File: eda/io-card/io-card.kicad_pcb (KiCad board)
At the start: 2 copper layers, 230 x 100 mm, 67 parts, among them J1 PS2, J2 Conn_02x25_Odd_Even, J3 PortA, J4 PortB, J5 ControlLines, J6 SPI, J7 Keyboard connector, J8 SD-Card module, J9 SD_Card, U1 W65C22SxP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

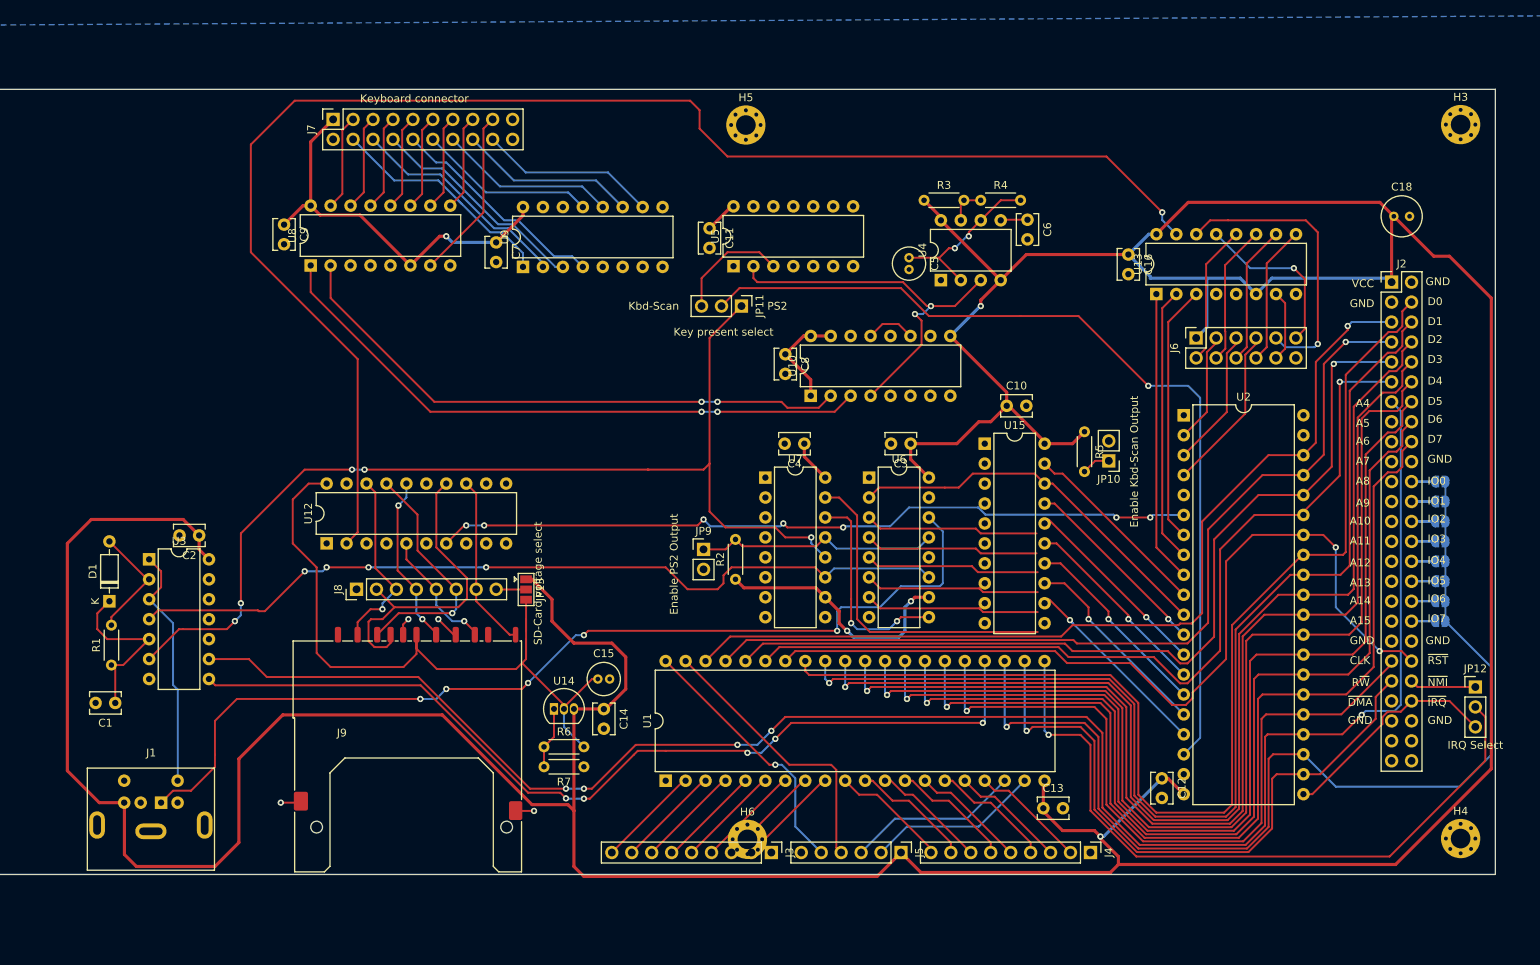
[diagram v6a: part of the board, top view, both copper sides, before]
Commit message: Rerouting IO card
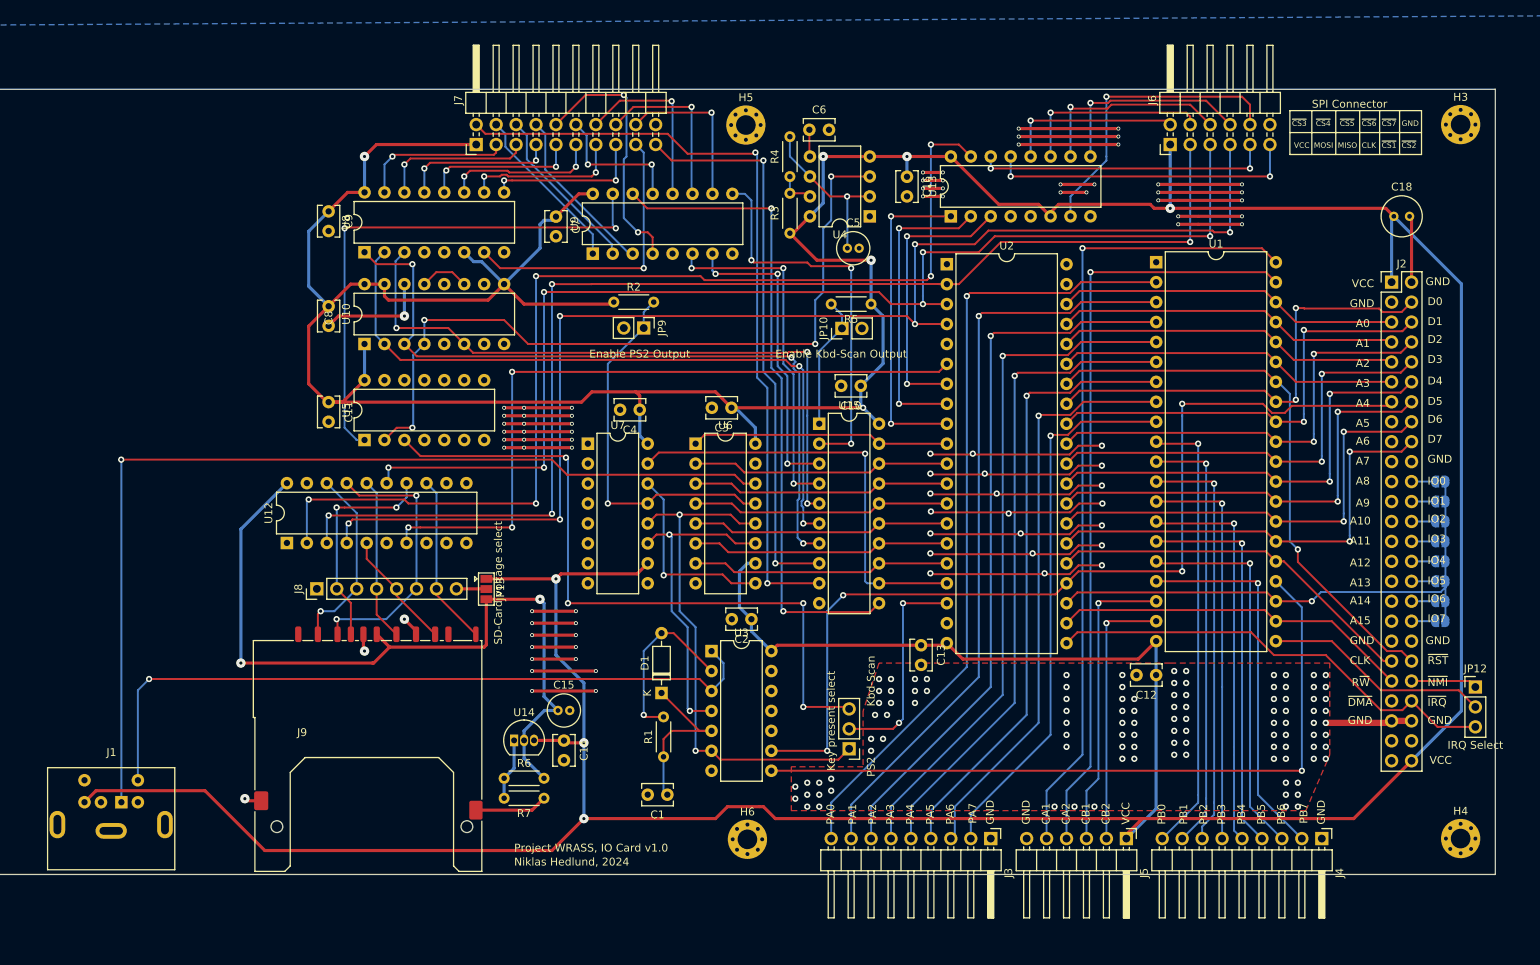
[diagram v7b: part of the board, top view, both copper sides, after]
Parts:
- J3, J4: footprint Connector_PinHeader_2.54mm:PinHeader_1x09_P2.54mm_Vertical -> Connector_PinHeader_2.54mm:PinHeader_1x09_P2.54mm_Horizontal
- J5: footprint Connector_PinHeader_2.54mm:PinHeader_1x06_P2.54mm_Vertical -> Connector_PinHeader_2.54mm:PinHeader_1x06_P2.54mm_Horizontal
- J6: footprint Connector_PinSocket_2.54mm:PinSocket_2x06_P2.54mm_Vertical -> Connector_PinHeader_2.54mm:PinHeader_2x06_P2.54mm_Horizontal
- J7: footprint Connector_PinSocket_2.54mm:PinSocket_2x10_P2.54mm_Vertical -> Connector_PinHeader_2.54mm:PinHeader_2x10_P2.54mm_Horizontal
- moved U1 90.9 mm to (202.9, 69.3), turned to 0 degrees
- moved U3 72.6 mm to (146.3, 118.9)
- moved D1 71.3 mm to (139.9, 124.2)
- moved C1 71.3 mm to (140.7, 137.2)
- moved R1 71.3 mm to (140.2, 132.3)
- moved C2 71.1 mm to (151.4, 114.8)
- moved C8 58.5 mm to (97.5, 75.0)
- moved JP11 58.0 mm to (163.8, 131.3), turned to 180 degrees
- moved U10 57.2 mm to (102.1, 79.8)
- moved C11 53.3 mm to (97.5, 87.2)
- moved U5 51.9 mm to (102.1, 92.0)
- moved R2 38.6 mm to (133.9, 74.4), turned to 0 degrees
- moved JP10 37.9 mm to (162.9, 77.8), turned to 90 degrees
- moved U2 35.8 mm to (176.3, 69.6)
- moved R5 31.7 mm to (166.6, 74.7), turned to 180 degrees
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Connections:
- J2 pad 47: unconnected-(J2-Pin_47-Pad47) -> /Expansion header/AudioL
- J2 pad 48: unconnected-(J2-Pin_48-Pad48) -> /Expansion header/~{ExtRomCs}
- J2 pad 49: unconnected-(J2-Pin_49-Pad49) -> /Expansion header/AudioR
- J2 pad 50: unconnected-(J2-Pin_50-Pad50) -> VCC
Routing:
- net GND: track 10.3 -> 407.3 mm, vias 4 -> 189
- net /SPI_CLK: track 21.3 -> 167.6 mm, vias 0 -> 6
- net /SPI_MOSI: track 14.1 -> 157.3 mm, vias 0 -> 4
- net /SPI_MISO: track 17.7 -> 151.9 mm, vias 0 -> 6
- net /Expansion header/A4: track 227.8 -> 121.3 mm, vias 5 -> 4
- net /Scanning keyboard interface/mod0: track 0.00 -> 99.3 mm, vias 0 -> 2
- net /Expansion header/D0: track 147.5 -> 57.7 mm, vias 0 -> 2
- net Net-(J3-Pin_9): track 13.2 -> 101.1 mm, vias 0 -> 1
- net /Expansion header/D1: track 145.0 -> 57.2 mm, vias 1 -> 2
- net Net-(JP11-C): track 114.0 -> 27.7 mm, vias 1 -> 2
- net /Expansion header/D2: track 142.6 -> 56.8 mm, vias 1 -> 2
- net /Scanning keyboard interface/Scancode2: track 0.00 -> 84.7 mm, vias 0 -> 3
- net Net-(J3-Pin_8): track 13.2 -> 96.6 mm, vias 0 -> 1
- net Net-(U15-Cp): track 0.00 -> 83.1 mm, vias 0 -> 2
- net /Expansion header/D3: track 139.7 -> 56.8 mm, vias 1 -> 2
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- added copper zone on F.Cu, net GND
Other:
- board text added: "A0"
- board text added: "A1"
- board text added: "A2"
- board text added: "A3"
- board text added: "CA1"
- board text added: "CA2"
- board text added: "CB1"
- board text added: "CB2"
- board text added: "MISO"
- board text added: "MOSI"
- board text added: "Niklas Hedlund, 2024"
- board text added: "PA0"
- board text added: "PA1"
- board text added: "PA2"
- board text added: "PA3"
- board text added: "PA4"
- board text added: "PA5"
- board text added: "PA6"
- board text added: "PA7"
- board text added: "PB0"
- board text added: "PB1"
- board text added: "PB2"
- board text added: "PB3"
- board text added: "PB4"
- board text added: "PB5"
- board text added: "PB6"
- board text added: "PB7"
- board text added: "Project WRASS, IO Card v1.0"
- board text added: "SPI Connector"
- board text added: "~{CS1}"
- board text added: "~{CS2}"
- board text added: "~{CS3}"
- board text added: "~{CS4}"
- board text added: "~{CS5}"
- board text added: "~{CS6}"
- board text added: "~{CS7}"

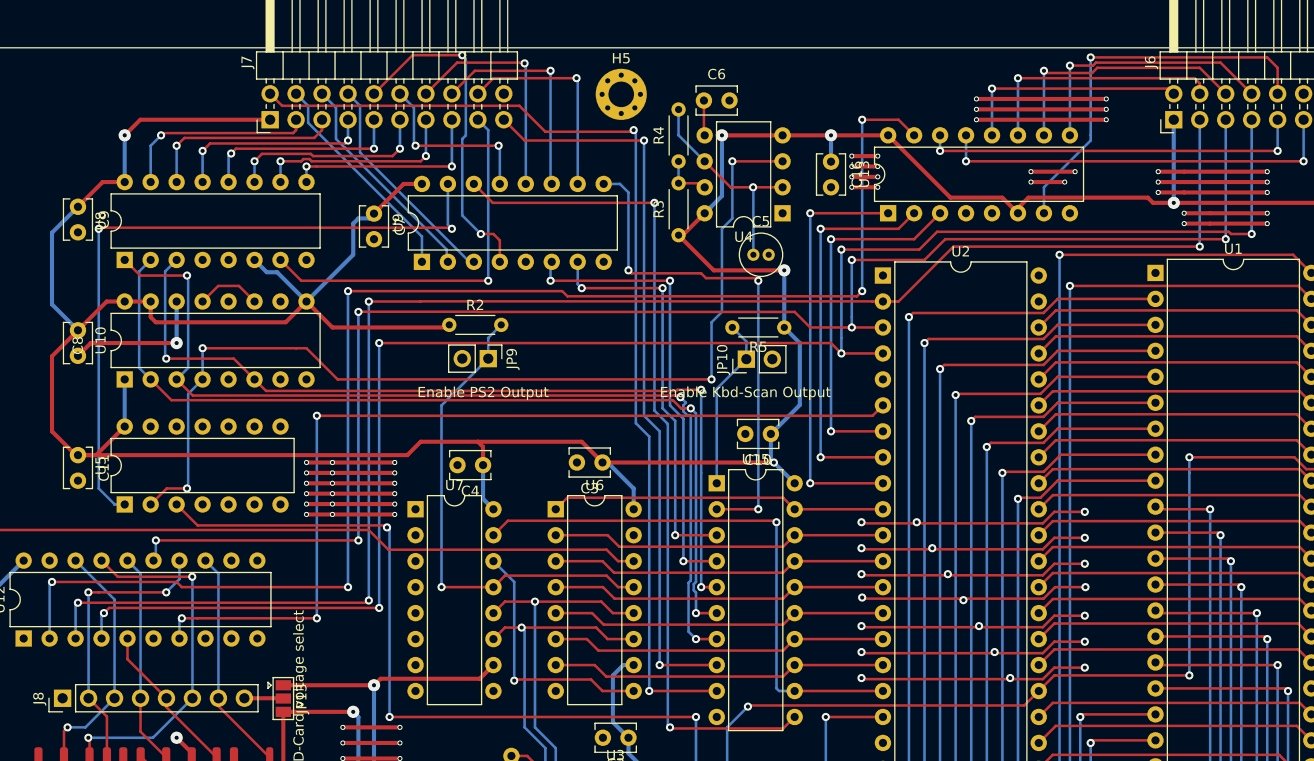
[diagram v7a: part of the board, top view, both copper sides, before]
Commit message: Work on SPI with actual hardware
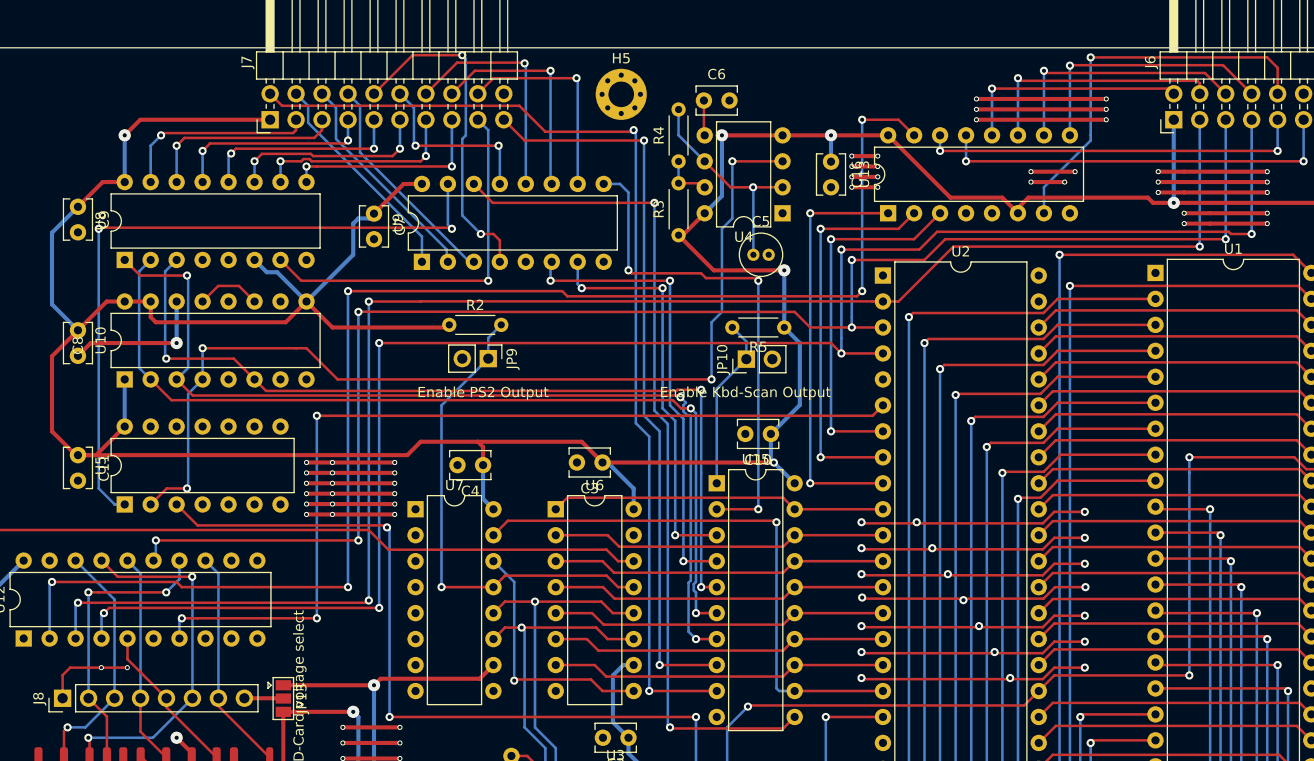
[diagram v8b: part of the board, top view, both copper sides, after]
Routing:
- net GND: track 407.3 -> 416.2 mm, vias 189 -> 191
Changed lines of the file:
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@@
 	)
 	(segment
+		(start 96.034 108.69)
+		(end 96.034 110.942)
+		(width 0.25)
+		(layer "F.Cu")
+		(net 71)
+	)
+	(segment
 		(start 123.444 116.84)
 		(end 129.032 116.84)
@@
 	)
 	(segment
+		(start 96.774 107.95)
+		(end 99.822 107.95)
+		(width 0.25)
+		(layer "F.Cu")
+		(net 71)
+	)
+	(segment
 		(start 196.021009 107.95)
 		(end 193.04 107.95)
@@
 	)
 	(segment
+		(start 96.774 107.95)
+		(end 96.034 108.69)
+		(width 0.25)
+		(layer "F.Cu")
+		(net 71)
+	)
+	(segment
 		(start 232.664 128.016)
 		(end 224.536 128.016)
@@
 	)
 	(segment
+		(start 99.822 107.95)
+		(end 101.893852 107.95)
+		(width 0.25)
+		(layer "F.Cu")
+		(net 71)
+	)
+	(segment
 		(start 181.211 96.375)
 		(end 181.102 96.266)
@@
 	)
 	(segment
+		(start 101.893852 107.95)
+		(end 102.362 107.95)
+		(width 0.25)
+		(layer "F.Cu")
+		(net 71)
+	)
+	(segment
 		(start 179.469 93.835)
 		(end 174.286009 93.835)
@@
 	)
 	(via
+		(at 99.822 107.95)
+		(size 0.5)
+		(drill 0.3)
+		(layers "F.Cu" "B.Cu")
+		(net 71)
+	)
+	(via
 		(at 195.072 59.436)
 		(size 0.5)
@@
 	)
 	(via
+		(at 102.362 107.95)
+		(size 0.5)
+		(drill 0.3)
+		(layers "F.Cu" "B.Cu")
+		(net 71)
+	)
+	(via
 		(at 205.232 129.032)
 		(size 0.8)
@@
 	)
 	(segment
-		(start 197.113305 48.768)
-		(end 209.296 48.768)
-		(width 0.25)
-		(layer "F.Cu")
-		(net 130)
-	)
-	(segment
-		(start 209.296 48.768)
-		(end 212.344 51.816)
+		(start 194.601 49.022)
+		(end 209.55 49.022)
 		(width 0.25)
 		(layer "F.Cu")
@@
 	(segment
 		(start 194.564 49.059)
-		(end 196.822305 49.059)
+		(end 194.601 49.022)
 		(width 0.25)
 		(layer "F.Cu")
@@
 	)
 	(segment
-		(start 196.822305 49.059)
-		(end 197.113305 48.768)
+		(start 209.55 49.022)
+		(end 212.344 51.816)
 		(width 0.25)
 		(layer "F.Cu")
@@
 	)
 	(segment
-		(start 192.241 49.784)
-		(end 196.733701 49.784)
-		(width 0.25)
-		(layer "F.Cu")
-		(net 131)
-	)
-	(segment
-		(start 196.733701 49.784)
-		(end 197.241701 49.276)
-		(width 0.25)
-		(layer "F.Cu")
-		(net 131)
-	)
-	(segment
-		(start 197.241701 49.276)
-		(end 207.264 49.276)
+		(start 207.772 49.784)
+		(end 209.804 51.816)
 		(width 0.25)
 		(layer "F.Cu")
@@
 	)
 	(segment
-		(start 207.264 49.276)
-		(end 209.804 51.816)
+		(start 192.241 49.784)
+		(end 207.772 49.784)
 		(width 0.25)
 		(layer "F.Cu")
@@
 	)
 	(segment
-		(start 206.756 50.292)
+		(start 207.264 50.8)
+		(end 207.264 51.816)
+		(width 0.25)
+		(layer "F.Cu")
+		(net 132)
+	)
+	(segment
+		(start 207.01 50.546)
 		(end 207.264 50.8)
 		(width 0.25)
@@
 	)
 	(segment
-		(start 207.264 50.8)
-		(end 207.264 51.816)
+		(start 189.738 50.546)
+		(end 207.01 50.546)
 		(width 0.25)
 		(layer "F.Cu")
@@
 	(segment
 		(start 189.484 50.292)
-		(end 206.756 50.292)
+		(end 189.738 50.546)
 		(width 0.25)
 		(layer "F.Cu")
@@
 		(polygon
 			(pts
-				(xy 225.044 120.396) (xy 204.724 120.396) (xy 204.724 120.396) (xy 198.628 120.396) (xy 198.628 120.396)
-				(xy 167.64 120.396) (xy 165.608 126.492) (xy 165.608 133.604) (xy 156.464 133.604) (xy 156.464 139.192)
-				(xy 221.996 139.192) (xy 225.044 132.08)
+				(xy 225.044 120.396) (xy 204.724 120.396) (xy 198.628 120.396) (xy 167.64 120.396) (xy 165.608 126.492)
+				(xy 165.608 133.604) (xy 156.464 133.604) (xy 156.464 139.192) (xy 221.996 139.192) (xy 225.044 132.08)
 			)
 		)
